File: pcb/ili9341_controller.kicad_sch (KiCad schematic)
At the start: 84 parts, among them J1 USB_B_Micro, J2 RP_SWD_CONN, Q1 NPN, Q2 NPN, Q3 NPN, SW1 RP_RST_SW, SW2 RP_USB_BOOT_SW, U1 ICE40UP5K-SG48ITR, U2 LM3880, U3 LD1117S33TR_SOT223, U4 LD1117S12TR_SOT223, U5 LD1117S25TR_SOT223, U6 RP2040, U7 W25Q128JVS, Y1 12MHz

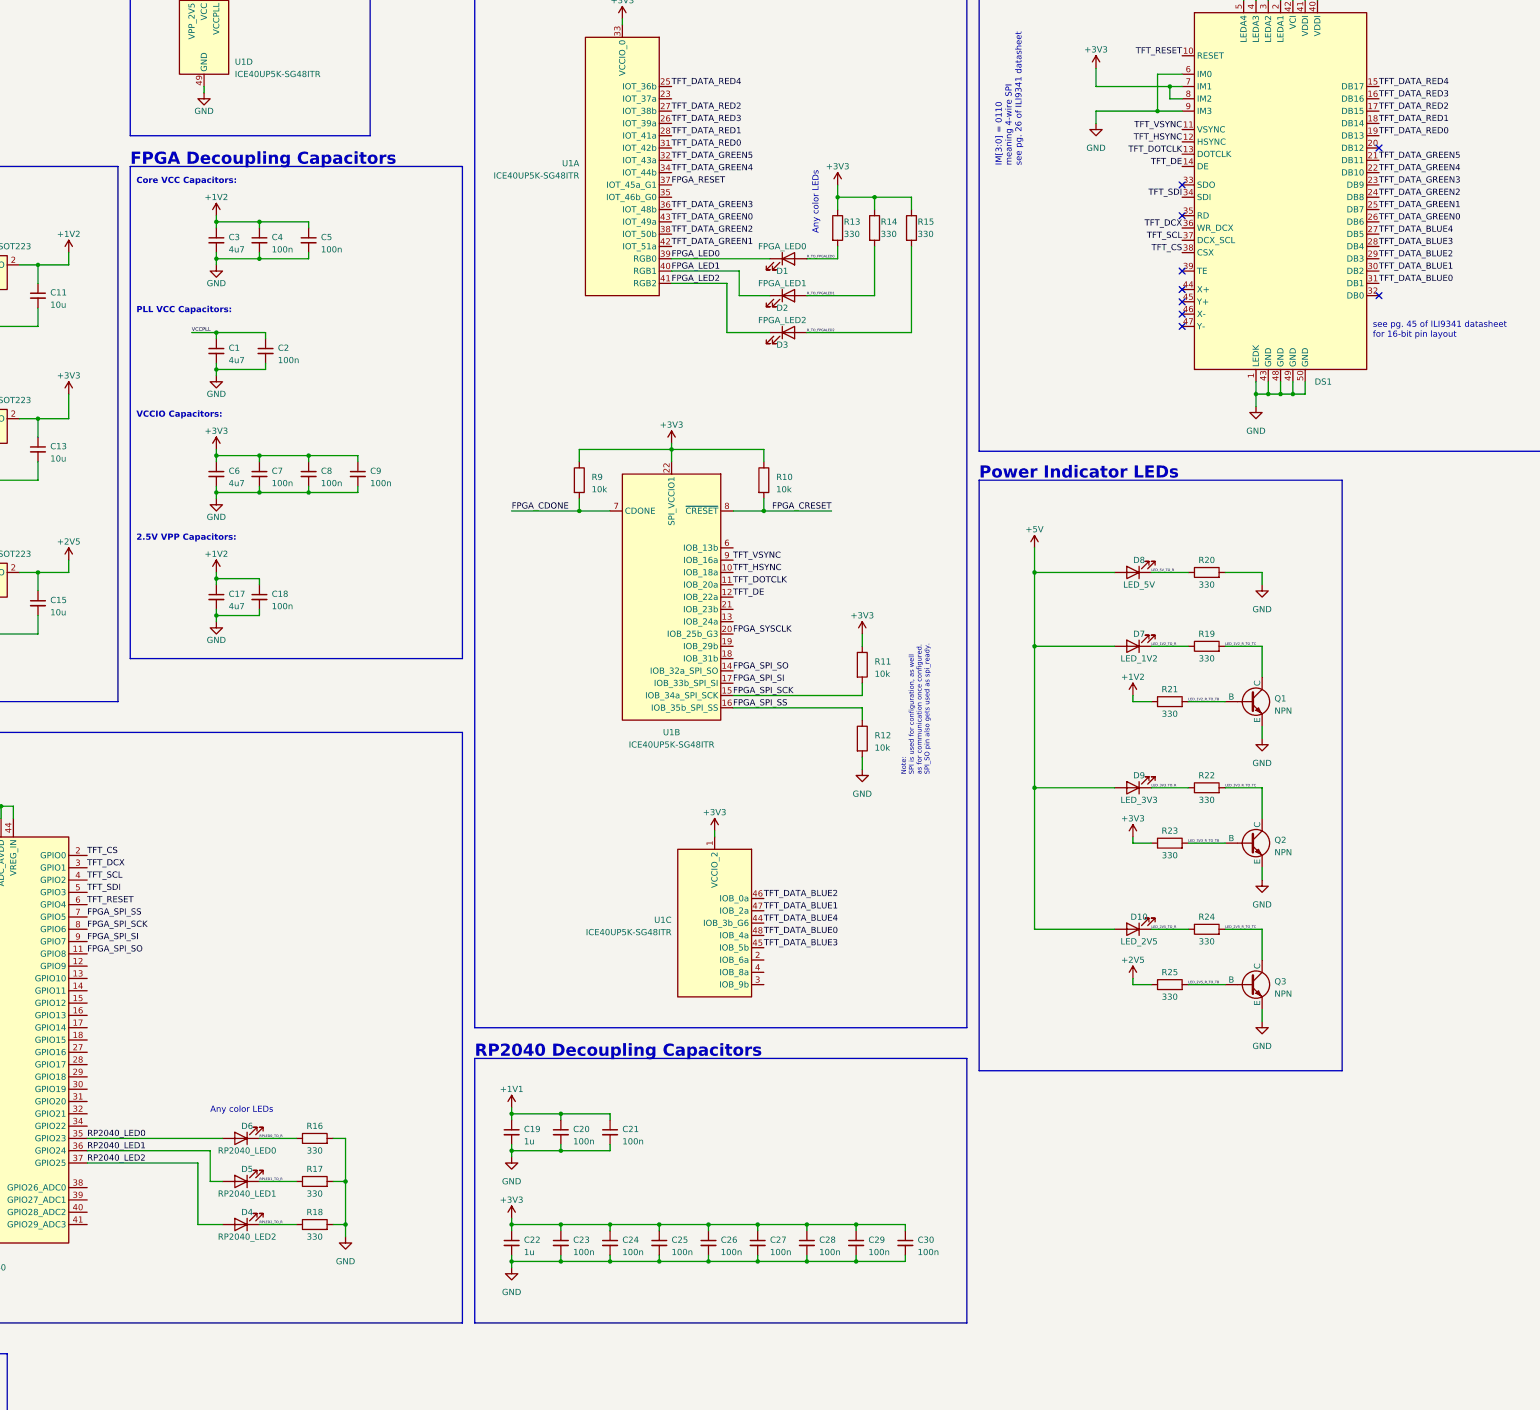
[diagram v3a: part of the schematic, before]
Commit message: add headers for unused pins
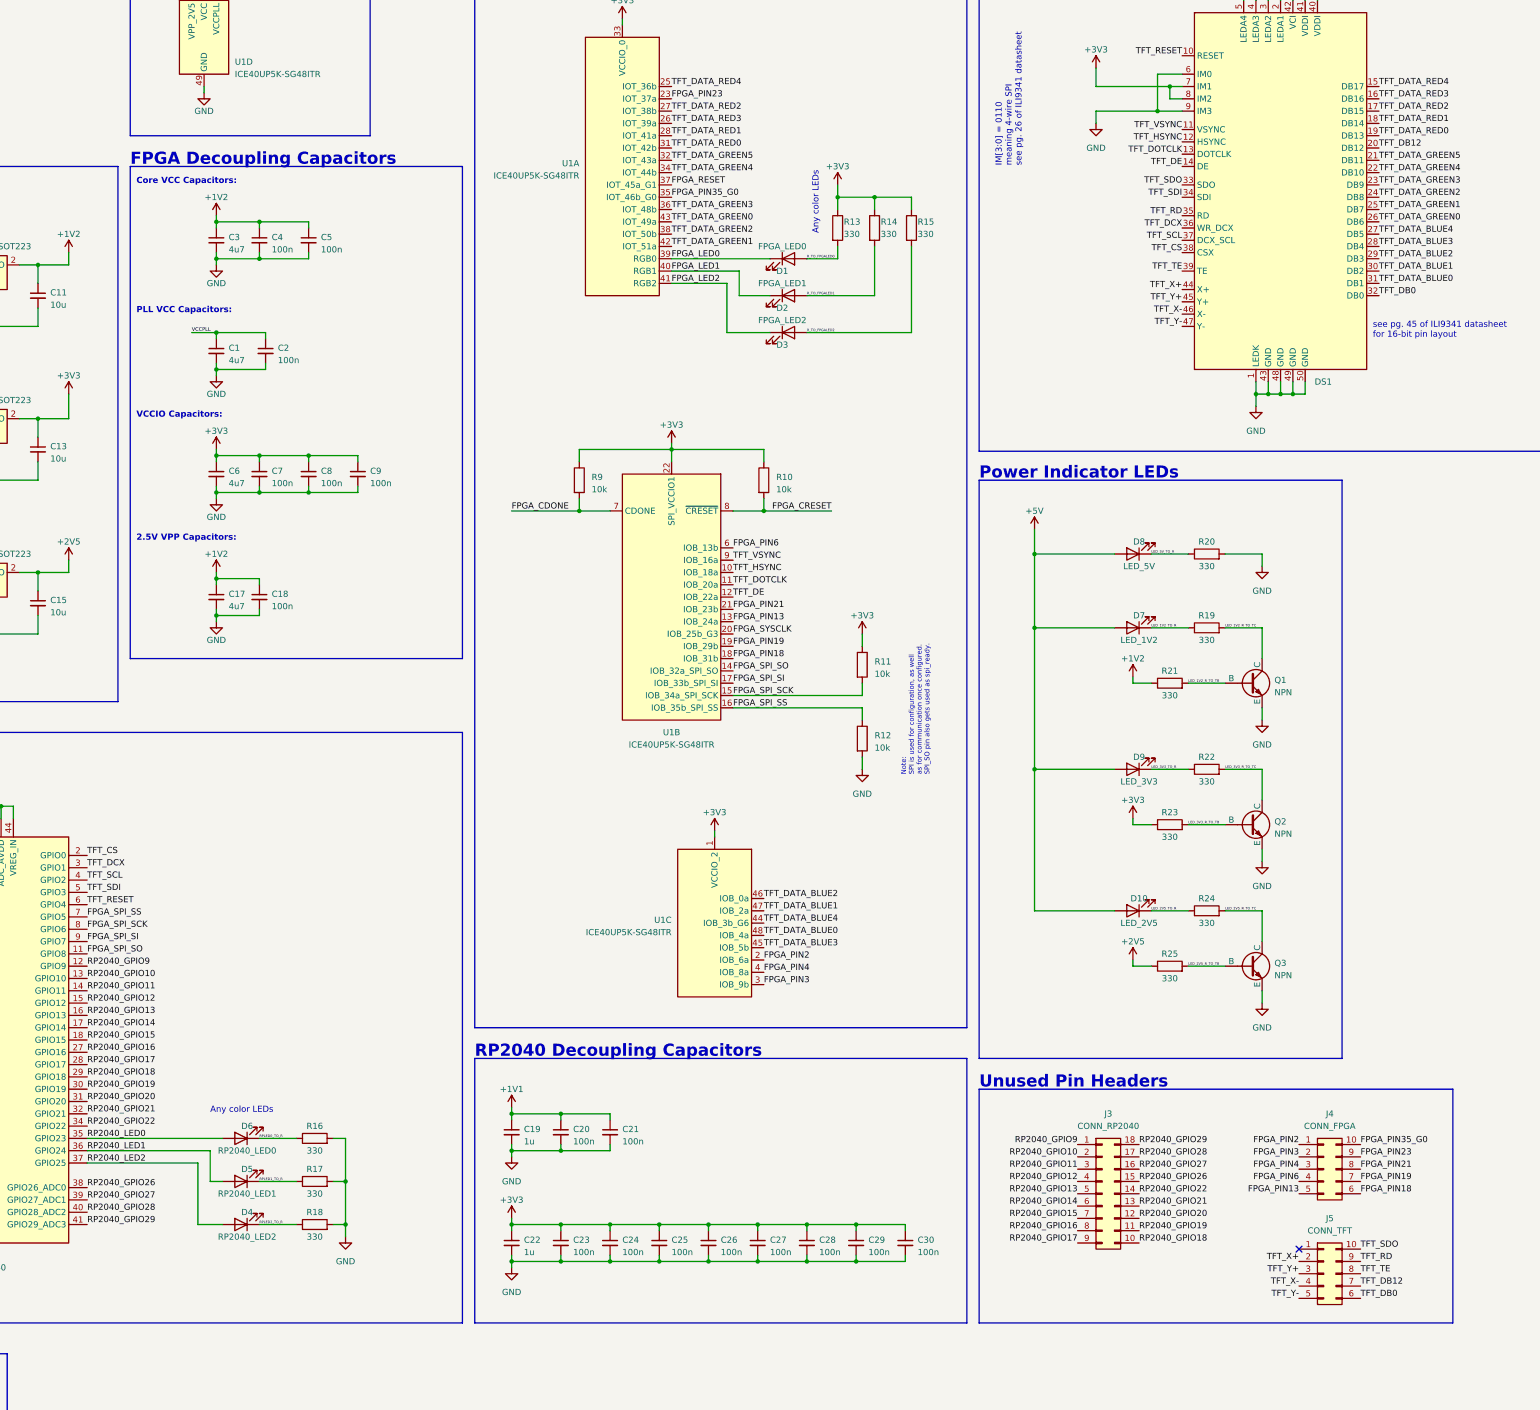
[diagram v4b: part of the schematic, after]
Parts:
- added J3: CONN_RP2040, symbol Connector_Generic:Conn_02x09_Counter_Clockwise
- added J4: CONN_FPGA, symbol Connector_Generic:Conn_02x05_Counter_Clockwise
- added J5: CONN_TFT, symbol Connector_Generic:Conn_02x05_Counter_Clockwise
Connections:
- net FPGA_PIN2: now reaches U1.2 (IOB_6a)
- net FPGA_PIN2: now also J4.1 (Pin_1)
- net FPGA_PIN3: now reaches U1.3 (IOB_9b)
- net FPGA_PIN3: now also J4.2 (Pin_2)
- net FPGA_PIN4: now reaches U1.4 (IOB_8a)
- net FPGA_PIN4: now also J4.3 (Pin_3)
- net FPGA_PIN13: now reaches U1.13 (IOB_24a)
- net FPGA_PIN13: now also J4.5 (Pin_5)
- net FPGA_PIN18: now reaches U1.18 (IOB_31b)
- net FPGA_PIN18: now also J4.6 (Pin_6)
- net FPGA_PIN19: now reaches U1.19 (IOB_29b)
- net FPGA_PIN19: now also J4.7 (Pin_7)
- net FPGA_PIN21: now reaches U1.21 (IOB_23b)
- net FPGA_PIN21: now also J4.8 (Pin_8)
- net FPGA_PIN6: now reaches U1.6 (IOB_13b)
- net FPGA_PIN6: now also J4.4 (Pin_4)
- net RP2040_GPIO9: now reaches U6.12 (GPIO9)
- net RP2040_GPIO9: now also J3.1 (Pin_1)
- net RP2040_GPIO10: now reaches U6.13 (GPIO10)
- net RP2040_GPIO10: now also J3.2 (Pin_2)
- net RP2040_GPIO11: now reaches U6.14 (GPIO11)
- net RP2040_GPIO11: now also J3.3 (Pin_3)
- net RP2040_GPIO12: now reaches U6.15 (GPIO12)
- net RP2040_GPIO12: now also J3.4 (Pin_4)
- net RP2040_GPIO13: now reaches U6.16 (GPIO13)
- net RP2040_GPIO13: now also J3.5 (Pin_5)
- net RP2040_GPIO14: now reaches U6.17 (GPIO14)
- net RP2040_GPIO14: now also J3.6 (Pin_6)
- net RP2040_GPIO15: now reaches U6.18 (GPIO15)
- net RP2040_GPIO15: now also J3.7 (Pin_7)
- net RP2040_GPIO16: now reaches U6.27 (GPIO16)
- net RP2040_GPIO16: now also J3.8 (Pin_8)
- net RP2040_GPIO17: now reaches U6.28 (GPIO17)
- net RP2040_GPIO17: now also J3.9 (Pin_9)
- net RP2040_GPIO18: now reaches U6.29 (GPIO18)
- net RP2040_GPIO18: now also J3.10 (Pin_10)
- net RP2040_GPIO19: now reaches U6.30 (GPIO19)
- net RP2040_GPIO19: now also J3.11 (Pin_11)
- net RP2040_GPIO20: now reaches U6.31 (GPIO20)
- net RP2040_GPIO20: now also J3.12 (Pin_12)
- net RP2040_GPIO21: now reaches U6.32 (GPIO21)
- net RP2040_GPIO21: now also J3.13 (Pin_13)
- net RP2040_GPIO22: now reaches U6.34 (GPIO22)
- net RP2040_GPIO22: now also J3.14 (Pin_14)
- net RP2040_GPIO26: now reaches U6.38 (GPIO26_ADC0)
- net RP2040_GPIO26: now also J3.15 (Pin_15)
- net RP2040_GPIO27: now reaches U6.39 (GPIO27_ADC1)
- net RP2040_GPIO27: now also J3.16 (Pin_16)
- net RP2040_GPIO28: now reaches U6.40 (GPIO28_ADC2)
- net RP2040_GPIO28: now also J3.17 (Pin_17)
- net RP2040_GPIO29: now reaches U6.41 (GPIO29_ADC3)
- net RP2040_GPIO29: now also J3.18 (Pin_18)
- net TFT_DB12: now reaches DS1.20 (DB12)
- net TFT_DB12: now also J5.7 (Pin_7)
- net TFT_DB0: now reaches DS1.32 (DB0)
- net TFT_DB0: now also J5.6 (Pin_6)
- net TFT_SDO: now reaches DS1.33 (SDO)
- net TFT_SDO: now also J5.10 (Pin_10)
- net TFT_RD: now reaches DS1.35 (RD)
- net TFT_RD: now also J5.9 (Pin_9)
- net TFT_TE: now reaches DS1.39 (TE)
- net TFT_TE: now also J5.8 (Pin_8)
- net TFT_X+: now reaches DS1.44 (X+)
- net TFT_X+: now also J5.2 (Pin_2)
- net TFT_Y+: now reaches DS1.45 (Y+)
- net TFT_Y+: now also J5.3 (Pin_3)
- net TFT_X-: now reaches DS1.46 (X-)
- net TFT_X-: now also J5.4 (Pin_4)
- net TFT_Y-: now reaches DS1.47 (Y-)
- net TFT_Y-: now also J5.5 (Pin_5)
- net FPGA_PIN23: now reaches U1.23 (IOT_37a)
- net FPGA_PIN23: now also J4.9 (Pin_9)
- net FPGA_PIN35_G0: now reaches U1.35 (IOT_46b_G0)
- net FPGA_PIN35_G0: now also J4.10 (Pin_10)
- no-connect marks 10 -> 2
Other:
- note added: "Unused Pin Headers"
- moved on the sheet: D10, D7, D8, D9, Q1, Q2, Q3, R19, R20, R21, R22, R23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
